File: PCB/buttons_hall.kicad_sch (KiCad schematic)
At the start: 92 parts, among them U1 ADC108S022CIMTX/NOPB, U10 DRV5053VAQDBZR, U11 DRV5053VAQDBZR, U12 DRV5053VAQDBZR, U13 DRV5053VAQDBZR, U14 DRV5053VAQDBZR, U15 DRV5053VAQDBZR, U16 DRV5053VAQDBZR, U17 DRV5053VAQDBZR, U18 DRV5053VAQDBZR, U19 DRV5053VAQDBZR, U3 ADC108S022CIMTX/NOPB, U4 DRV5053VAQDBZR, U5 DRV5053VAQDBZR, U6 DRV5053VAQDBZR, U7 DRV5053VAQDBZR, U8 DRV5053VAQDBZR, U9 DRV5053VAQDBZR

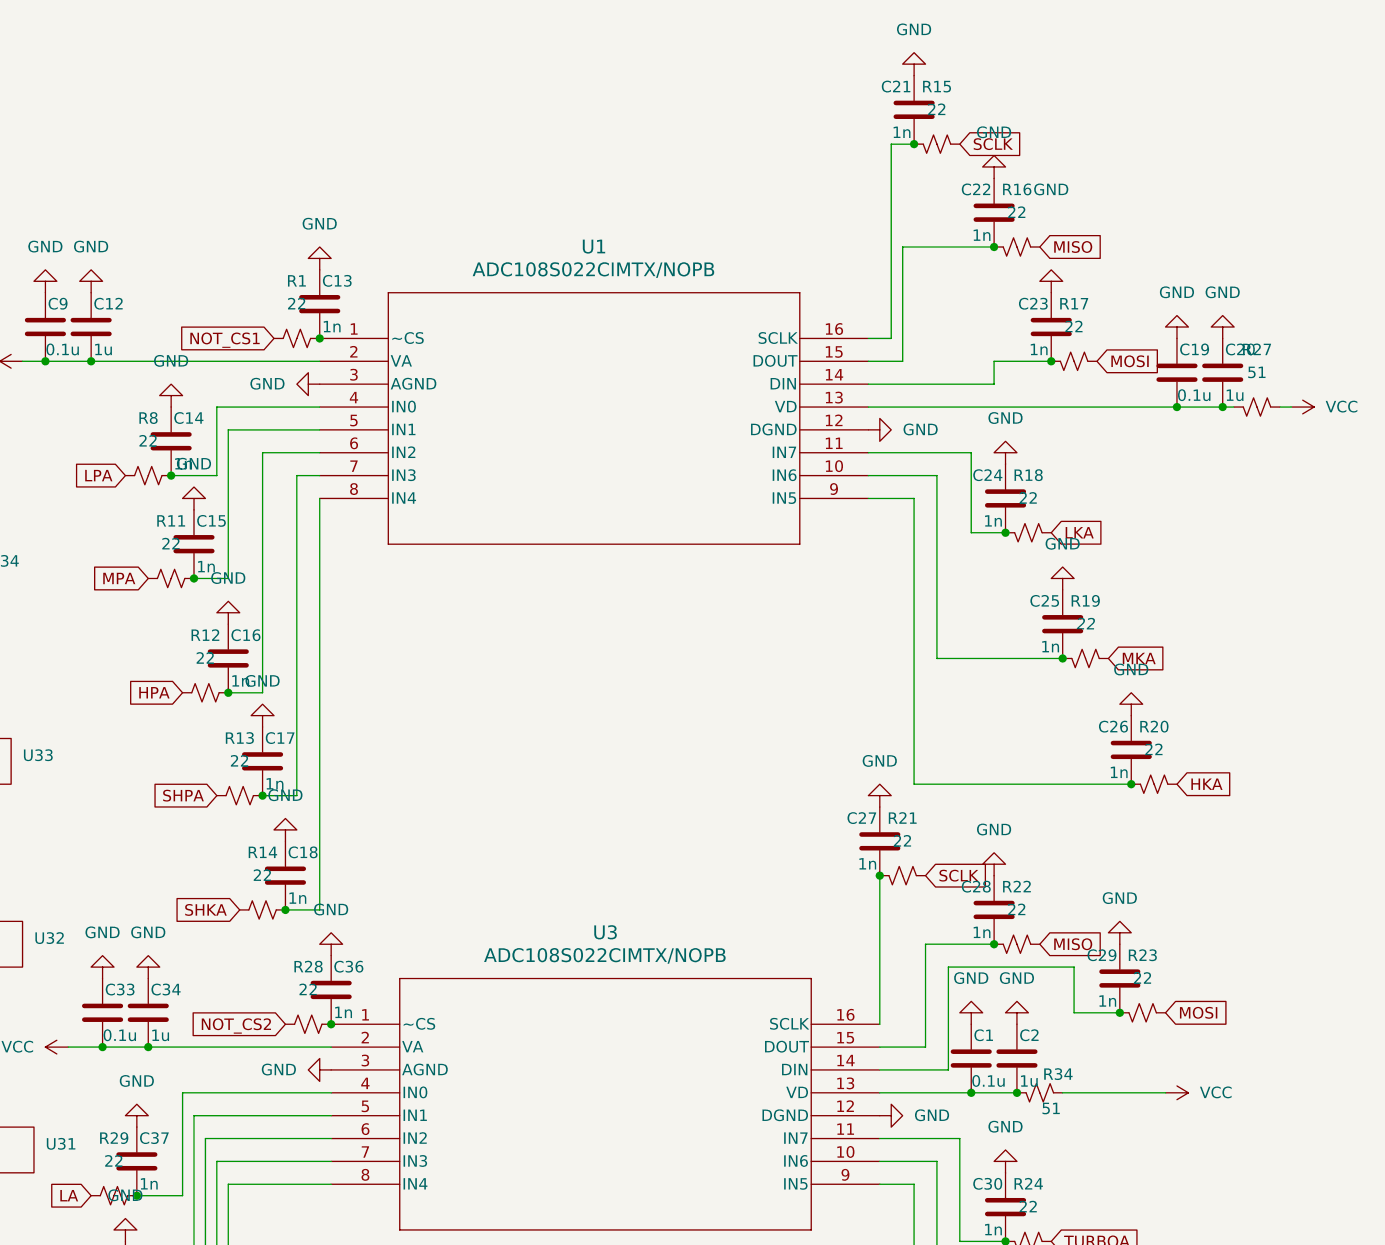
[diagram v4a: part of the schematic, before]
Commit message: PCB Updated to include the ADC improved components
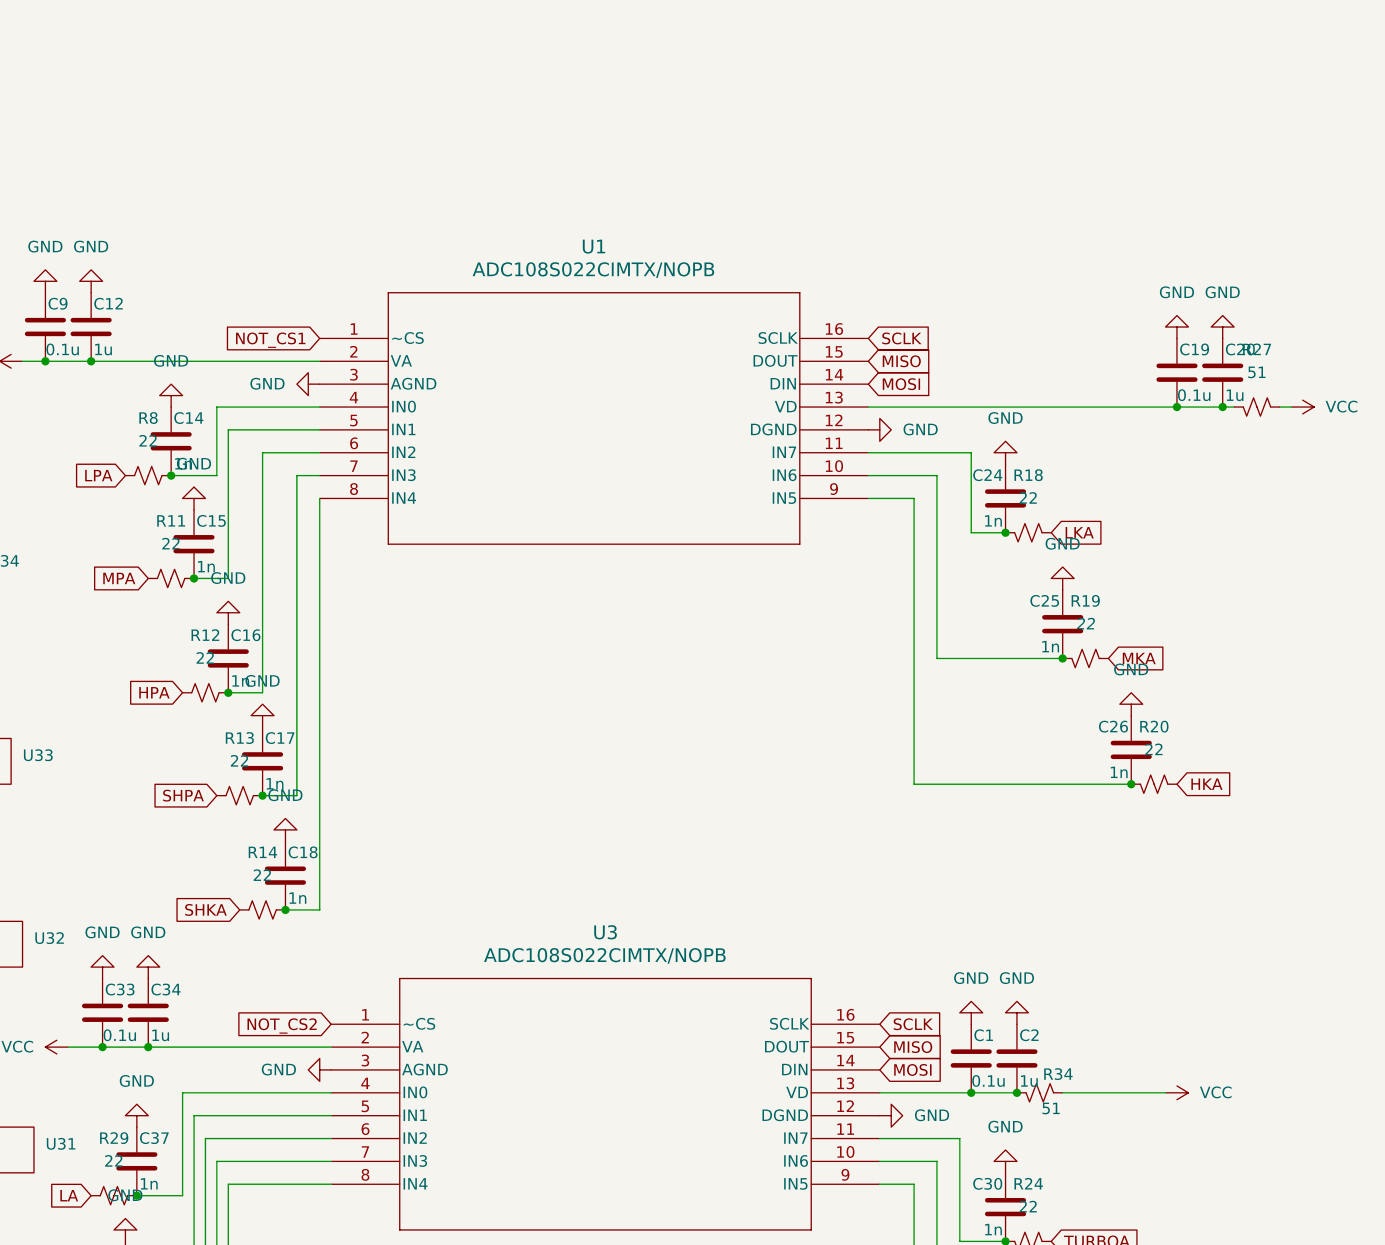
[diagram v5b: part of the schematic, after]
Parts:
- removed C13, C21, C22, C23, C27, C28, C29, C36: 1n, Capacitor_SMD:C_0603_1608Metric, symbol Device:C
- removed R1, R15, R16, R17, R21, R22, R23, R28: 22, Resistor_SMD:R_0603_1608Metric, symbol Device:R_Small_US
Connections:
- net MISO: now also U1.15 (DOUT), U3.15 (DOUT)
- net MOSI: now also U1.14 (DIN), U3.14 (DIN)
- net NOT_CS1: now also U1.1 (~CS)
- net NOT_CS2: now also U3.1 (~CS)
- net SCLK: now also U1.16 (SCLK), U3.16 (SCLK)
